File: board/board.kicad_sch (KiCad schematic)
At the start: 8 parts, among them J1 007_ADC, J2 Conn_01x02_Male, J3 007_ADC

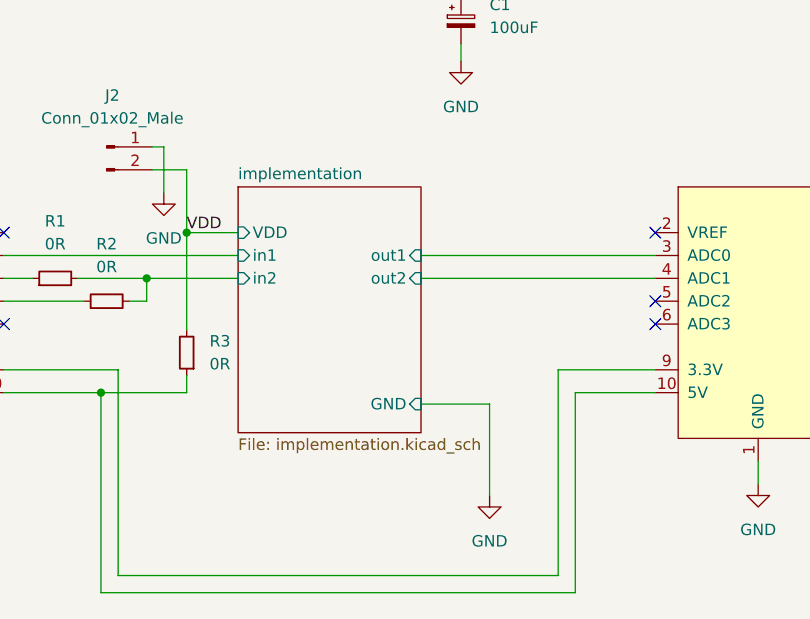
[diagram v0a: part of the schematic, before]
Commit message: added missing schemetic
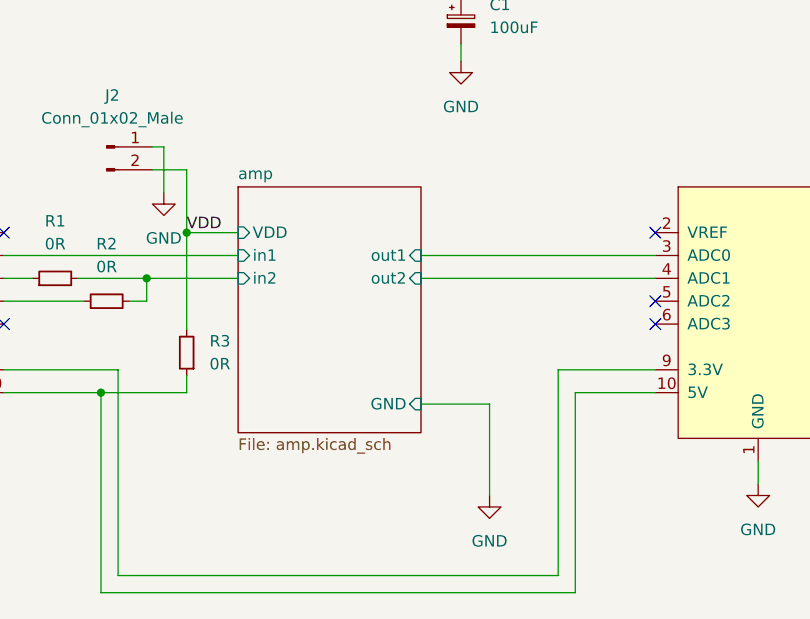
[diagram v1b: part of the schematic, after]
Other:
- sheet implementation renamed amp
- sheet amp: file implementation.kicad_sch -> amp.kicad_sch
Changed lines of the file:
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@@
     (stroke (width 0.1524) (type solid) (color 0 0 0 0))
     (fill (color 0 0 0 0.0000))
-    (property "Sheet name" "implementation" (id 0) (at 154.94 104.6984 0)
+    (property "Sheet name" "amp" (id 0) (at 154.94 104.6984 0)
       (effects (font (size 1.27 1.27)) (justify left bottom))
     )
-    (property "Sheet file" "implementation.kicad_sch" (id 1) (at 154.94 133.2996 0)
+    (property "Sheet file" "amp.kicad_sch" (id 1) (at 154.94 133.2996 0)
       (effects (font (size 1.27 1.27)) (justify left top))
     )
@@
       (reference "C1") (unit 1) (value "100uF") (footprint "Capacitor_SMD:CP_Elec_8x6.9")
     )
-    (path "/767ce4c6-0e55-4543-92f0-34cb8237a544/c47ceec0-c44a-43b1-98df-edd18a9e402b"
+    (path "/767ce4c6-0e55-4543-92f0-34cb8237a544/54b9f432-c78d-442d-9a66-21ee06e48126"
       (reference "C2") (unit 1) (value "1uF") (footprint "Capacitor_SMD:C_0805_2012Metric")
     )
@@
       (reference "R3") (unit 1) (value "0R") (footprint "Resistor_SMD:R_0603_1608Metric")
     )
-    (path "/767ce4c6-0e55-4543-92f0-34cb8237a544/e2246c92-27d3-4e39-90dc-1d91c5dee04d"
+    (path "/767ce4c6-0e55-4543-92f0-34cb8237a544/49487811-510d-478d-bfce-f7327255ac51"
       (reference "R6") (unit 1) (value "0R") (footprint "Resistor_SMD:R_0603_1608Metric")
     )
-    (path "/767ce4c6-0e55-4543-92f0-34cb8237a544/5602285e-702e-425e-9b5a-81920ed82fda"
+    (path "/767ce4c6-0e55-4543-92f0-34cb8237a544/187b62f1-7248-4e99-8d86-fd15117b686e"
       (reference "R7") (unit 1) (value "0R") (footprint "Resistor_SMD:R_0603_1608Metric")
     )
-    (path "/767ce4c6-0e55-4543-92f0-34cb8237a544/d94d6e77-7d98-4ed7-955c-312429317647"
+    (path "/767ce4c6-0e55-4543-92f0-34cb8237a544/d145e977-8965-4243-bc54-2e172a5118fb"
       (reference "R8") (unit 1) (value "d.n.p") (footprint "Resistor_SMD:R_0603_1608Metric")
     )
-    (path "/767ce4c6-0e55-4543-92f0-34cb8237a544/524998fd-7705-4b76-8ab2-ed43b7904494"
+    (path "/767ce4c6-0e55-4543-92f0-34cb8237a544/f3d66dfb-f2d3-4655-9541-1fcf0f70c054"
       (reference "R9") (unit 1) (value "d.n.p") (footprint "Resistor_SMD:R_0603_1608Metric")
     )
-    (path "/767ce4c6-0e55-4543-92f0-34cb8237a544/f80e5109-b03a-455f-88e1-0da650aef011"
+    (path "/767ce4c6-0e55-4543-92f0-34cb8237a544/bf54471e-15bb-464d-8744-3cc9d0b18d5d"
       (reference "R10") (unit 1) (value "d.n.p") (footprint "Resistor_SMD:R_0603_1608Metric")
     )
-    (path "/767ce4c6-0e55-4543-92f0-34cb8237a544/582be712-b9a8-4b16-ab1f-e6c3f535bc48"
+    (path "/767ce4c6-0e55-4543-92f0-34cb8237a544/1b48fc4e-467e-4bed-ae00-a09d76211fe1"
       (reference "R11") (unit 1) (value "d.n.p") (footprint "Resistor_SMD:R_0603_1608Metric")
     )
-    (path "/767ce4c6-0e55-4543-92f0-34cb8237a544/b01b0d42-4219-49f1-9026-37aec135e25c"
+    (path "/767ce4c6-0e55-4543-92f0-34cb8237a544/f6cbb0a3-f36d-4496-b51e-8d0d45a504de"
       (reference "R12") (unit 1) (value "0R") (footprint "Resistor_SMD:R_0603_1608Metric")
     )
-    (path "/767ce4c6-0e55-4543-92f0-34cb8237a544/8fe11dde-26fc-468f-9a55-f087d4d8042a"
+    (path "/767ce4c6-0e55-4543-92f0-34cb8237a544/250bc2b1-661c-4036-8c27-63b8442bee34"
       (reference "R13") (unit 1) (value "0R") (footprint "Resistor_SMD:R_0603_1608Metric")
     )
-    (path "/767ce4c6-0e55-4543-92f0-34cb8237a544/89bf35a9-7cb7-4d9f-9a5b-7f6befcae6b0"
+    (path "/767ce4c6-0e55-4543-92f0-34cb8237a544/9643f1c3-8d9a-41ba-a17e-210f9f76a6e4"
       (reference "U1") (unit 1) (value "TCA0372") (footprint "Package_SO:SOIC-16W_7.5x10.3mm_P1.27mm")
     )
-    (path "/767ce4c6-0e55-4543-92f0-34cb8237a544/39ce7da2-7a88-4e79-85f2-2d6da143a668"
+    (path "/767ce4c6-0e55-4543-92f0-34cb8237a544/e77f807e-80fa-47c2-b1b1-7a9482efd23b"
       (reference "U1") (unit 2) (value "TCA0372") (footprint "Package_SO:SOIC-16W_7.5x10.3mm_P1.27mm")
     )
-    (path "/767ce4c6-0e55-4543-92f0-34cb8237a544/8453af24-34c7-4e49-8dd8-eda861208fd7"
+    (path "/767ce4c6-0e55-4543-92f0-34cb8237a544/25629c1a-b954-414b-889a-67369ecc2252"
       (reference "U1") (unit 3) (value "TCA0372") (footprint "Package_SO:SOIC-16W_7.5x10.3mm_P1.27mm")
     )
